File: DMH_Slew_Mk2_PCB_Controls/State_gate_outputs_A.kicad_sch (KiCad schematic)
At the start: 25 parts, among them J10 TS_Jack_6.35mm_Sw, J9 TS_Jack_6.35mm_Sw, Q11 BC548, Q12 BC548, U3 TL074

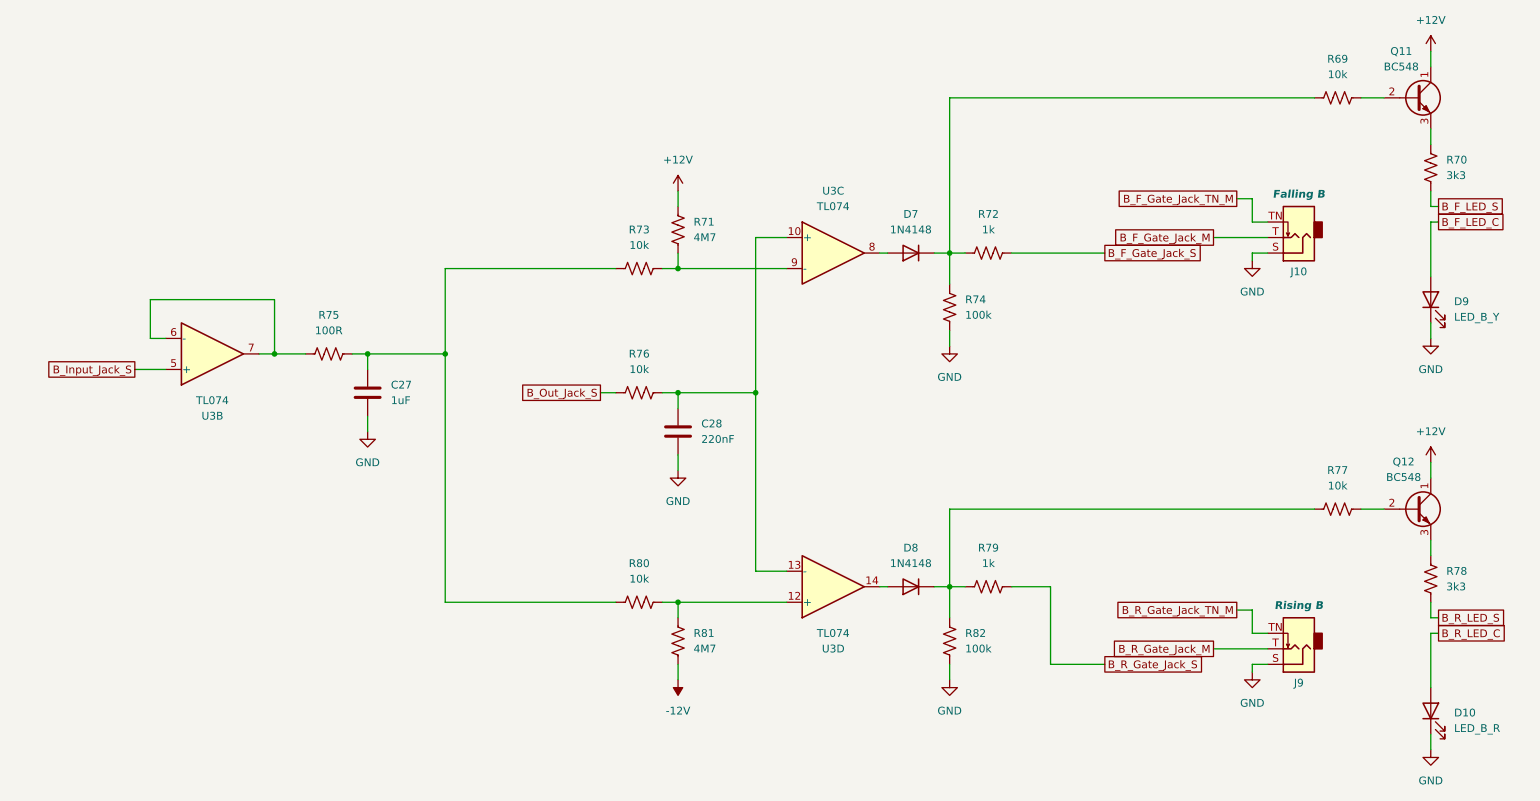
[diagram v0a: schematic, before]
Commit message: Designed Controls PCB
... and removed Mod feature
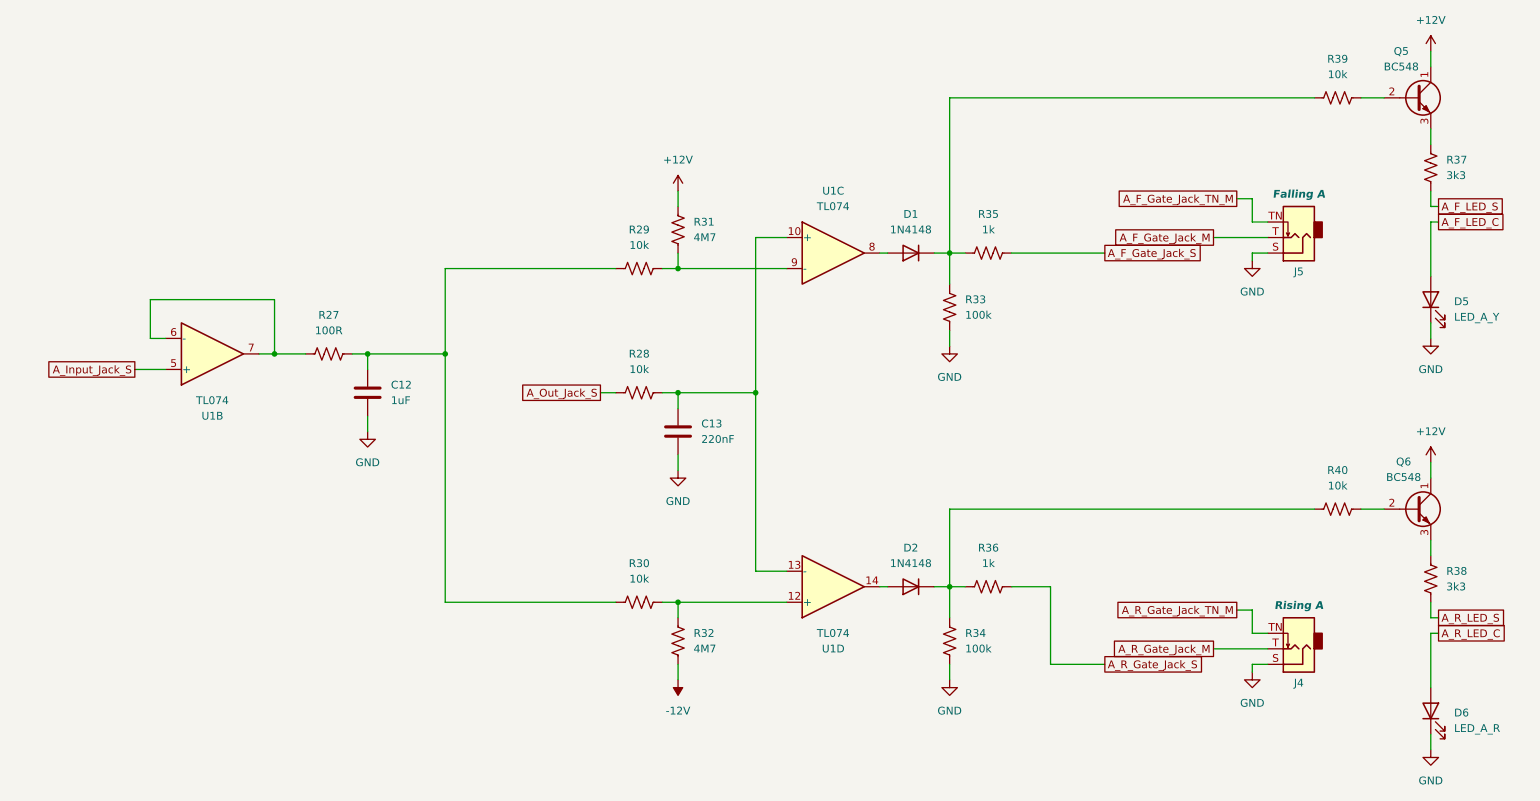
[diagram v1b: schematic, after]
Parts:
- removed C27: 1uF, Capacitor_THT:C_Disc_D4.3mm_W1.9mm_P5.00mm, symbol Device:C
- removed C28: 220nF, Capacitor_THT:C_Disc_D4.3mm_W1.9mm_P5.00mm, symbol Device:C
- removed D10: LED_B_R, LED_THT:LED_D3.0mm, symbol Device:LED
- removed D7, D8: 1N4148, Diode_THT:D_DO-35_SOD27_P7.62mm_Horizontal, symbol Diode:1N4148
- removed D9: LED_B_Y, LED_THT:LED_D3.0mm, symbol Device:LED
- removed J10, J9: TS_Jack_6.35mm_Sw, SynthStuff:CUI_MJ-63052A, symbol SynthStuff:TS_Jack_6.35mm_Sw
- removed Q11, Q12: BC548, Package_TO_SOT_THT:TO-92_Inline, symbol Transistor_BJT:BC548
- removed R69, R73, R76, R77, R80: 10k, Resistor_THT:R_Axial_DIN0207_L6.3mm_D2.5mm_P7.62mm_Horizontal, symbol Device:R_US
- removed R70, R78: 3k3, Resistor_THT:R_Axial_DIN0207_L6.3mm_D2.5mm_P7.62mm_Horizontal, symbol Device:R_US
- removed R71, R81: 4M7, Resistor_THT:R_Axial_DIN0207_L6.3mm_D2.5mm_P7.62mm_Horizontal, symbol Device:R_US
- removed R72, R79: 1k, Resistor_THT:R_Axial_DIN0207_L6.3mm_D2.5mm_P7.62mm_Horizontal, symbol Device:R_US
- removed R74, R82: 100k, Resistor_THT:R_Axial_DIN0207_L6.3mm_D2.5mm_P7.62mm_Horizontal, symbol Device:R_US
- removed R75: 100R, Resistor_THT:R_Axial_DIN0207_L6.3mm_D2.5mm_P7.62mm_Horizontal, symbol Device:R_US
- removed U3: TL074, Package_DIP:DIP-14_W7.62mm_Socket, symbol Amplifier_Operational:TL074
- added C12: 1uF, Capacitor_THT:C_Disc_D4.3mm_W1.9mm_P5.00mm, symbol Device:C
- added C13: 220nF, Capacitor_THT:C_Disc_D4.3mm_W1.9mm_P5.00mm, symbol Device:C
- added D1, D2: 1N4148, Diode_THT:D_DO-35_SOD27_P7.62mm_Horizontal, symbol Diode:1N4148
- added D5: LED_A_Y, LED_THT:LED_D3.0mm, symbol Device:LED
- added D6: LED_A_R, LED_THT:LED_D3.0mm, symbol Device:LED
- added J4, J5: TS_Jack_6.35mm_Sw, SynthStuff:CUI_MJ-63052A, symbol SynthStuff:TS_Jack_6.35mm_Sw
- added Q5, Q6: BC548, Package_TO_SOT_THT:TO-92_Inline, symbol Transistor_BJT:BC548
- added R27: 100R, Resistor_THT:R_Axial_DIN0207_L6.3mm_D2.5mm_P7.62mm_Horizontal, symbol Device:R_US
- added R28, R29, R30, R39, R40: 10k, Resistor_THT:R_Axial_DIN0207_L6.3mm_D2.5mm_P7.62mm_Horizontal, symbol Device:R_US
- added R31, R32: 4M7, Resistor_THT:R_Axial_DIN0207_L6.3mm_D2.5mm_P7.62mm_Horizontal, symbol Device:R_US
- added R33, R34: 100k, Resistor_THT:R_Axial_DIN0207_L6.3mm_D2.5mm_P7.62mm_Horizontal, symbol Device:R_US
- added R35, R36: 1k, Resistor_THT:R_Axial_DIN0207_L6.3mm_D2.5mm_P7.62mm_Horizontal, symbol Device:R_US
- added R37, R38: 3k3, Resistor_THT:R_Axial_DIN0207_L6.3mm_D2.5mm_P7.62mm_Horizontal, symbol Device:R_US
- added U1: TL074, Package_DIP:DIP-14_W7.62mm_Socket, symbol Amplifier_Operational:TL074
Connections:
- net +12V: now also Q5.1 (C), Q6.1 (C), R31.1
- net -12V: now also R32.2
- net GND: now also C12.2, C13.2, D5.1 (K), D6.1 (K), J4.S, J5.S, R33.2, R34.2
- new net: C13.1, R28.1, U1.10 (+), U1.13 (-)
- new net: D1.2 (A), U1.8
- new net: R29.1, R31.2, U1.9 (-)
- new net: Q6.2 (B), R40.1
- new net: D2.1 (K), R34.1, R36.2, R40.2
- new net: R30.1, R32.1, U1.12 (+)
- new net: D2.2 (A), U1.14
- new net: Q5.2 (B), R39.1
- new net: Q5.3 (E), R37.1
- new net: D1.1 (K), R33.1, R35.2, R39.2
- new net: R27.2, U1.6 (-), U1.7
- new net: Q6.3 (E), R38.1
- new net: C12.1, R27.1, R29.2, R30.2
- new net A_F_Gate_Jack_M: J5.T
- new net A_F_Gate_Jack_S: R35.1
- new net A_F_Gate_Jack_TN_M: J5.TN
- new net A_F_LED_C: D5.2 (A)
- new net A_F_LED_S: R37.2
- new net A_Input_Jack_S: U1.5 (+)
- new net A_Out_Jack_S: R28.2
- new net A_R_Gate_Jack_M: J4.T
- new net A_R_Gate_Jack_S: R36.1
- new net A_R_Gate_Jack_TN_M: J4.TN
- new net A_R_LED_C: D6.2 (A)
- new net A_R_LED_S: R38.2
